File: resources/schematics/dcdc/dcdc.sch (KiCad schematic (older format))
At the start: 21 parts

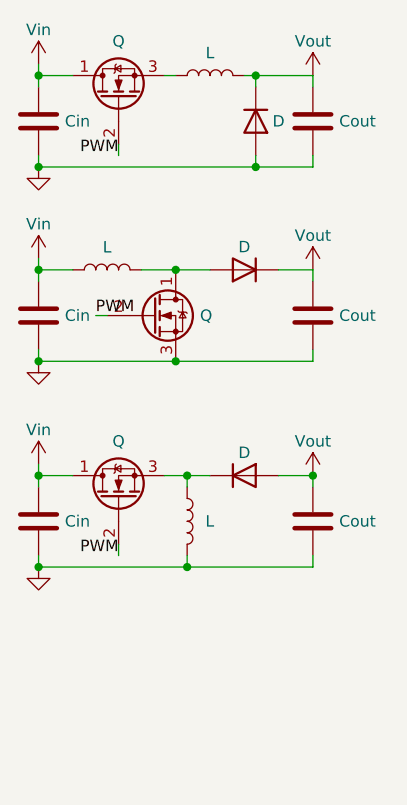
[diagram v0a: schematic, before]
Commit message: Add voltage divider diagram & minify svg
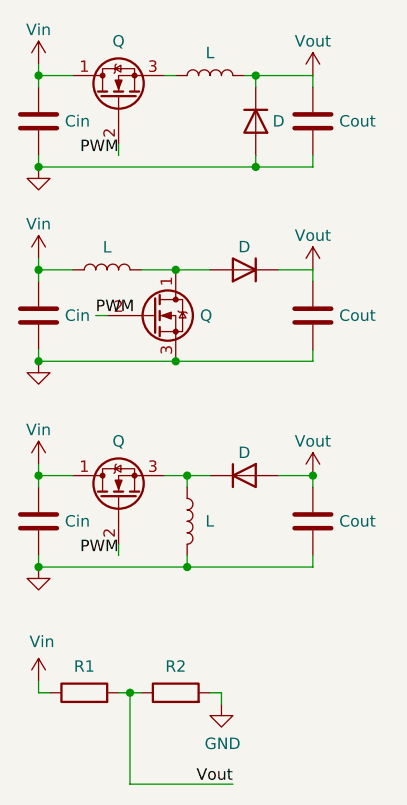
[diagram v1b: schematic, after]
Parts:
- added R1, R2: R, symbol Device:R
- added Vin: +12V, symbol power:+12V
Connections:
- net +12V: now also R1.1, Vin.1 (+12V)
- net GND: now also R2.2
- new net Vout: R1.2, R2.1
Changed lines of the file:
@@
 Connection ~ 650  2550
-$Comp
-L power:+12V Vin
-U 1 1 5DD46F62
-P 650 2500
-F 0 "Vin" H 650 2650 50  0000 C CNN
-F 1 "+12V" H 665 2673 50  0001 C CNN
-F 2 "" H 650 2500 50  0001 C CNN
-F 3 "" H 650 2500 50  0001 C CNN
-	1    650  2500
-	1    0    0    -1
-$EndComp
 $Comp
 L power:+12V Vout
@@
 	1    0    0    -1
 $EndComp
+$Comp
+L power:GND #PWR?
+U 1 1 5FDFFD01
+P 1450 3550
+F 0 "#PWR?" H 1450 3300 50  0001 C CNN
+F 1 "GND" H 1455 3377 50  0000 C CNN
+F 2 "" H 1450 3550 50  0001 C CNN
+F 3 "" H 1450 3550 50  0001 C CNN
+	1    1450 3550
+	1    0    0    -1
+$EndComp
+Wire Wire Line
+	1400 3500 1450 3500
+Wire Wire Line
+	1450 3500 1450 3550
+Wire Wire Line
+	700  3500 650  3500
+Wire Wire Line
+	650  3500 650  3450
+Wire Wire Line
+	1000 3500 1050 3500
+Wire Wire Line
+	1050 3500 1050 3900
+Wire Wire Line
+	1050 3900 1500 3900
+Connection ~ 1050 3500
+Wire Wire Line
+	1050 3500 1100 3500
+Text Label 1500 3900 2    50   ~ 0
+Vout
+$Comp
+L power:+12V Vin
+U 1 1 5DD46F62
+P 650 2500
+F 0 "Vin" H 650 2650 50  0000 C CNN
+F 1 "+12V" H 665 2673 50  0001 C CNN
+F 2 "" H 650 2500 50  0001 C CNN
+F 3 "" H 650 2500 50  0001 C CNN
+	1    650  2500
+	1    0    0    -1
+$EndComp
+$Comp
+L Device:R R2
+U 1 1 5FDFF45A
+P 1250 3500
+F 0 "R2" V 1365 3500 50  0000 C CNN
+F 1 "R" H 1320 3455 50  0001 L CNN
+F 2 "" V 1180 3500 50  0001 C CNN
+F 3 "~" H 1250 3500 50  0001 C CNN
+	1    1250 3500
+	0    -1   -1   0
+$EndComp
+$Comp
+L Device:R R1
+U 1 1 5FDFE9AA
+P 850 3500
+F 0 "R1" V 965 3500 50  0000 C CNN
+F 1 "R" H 920 3455 50  0001 L CNN
+F 2 "" V 780 3500 50  0001 C CNN
+F 3 "~" H 850 3500 50  0001 C CNN
+	1    850  3500
+	0    -1   -1   0
+$EndComp
+$Comp
+L power:+12V Vin
+U 1 1 5FE069E1
+P 650 3450
+F 0 "Vin" H 665 3623 50  0000 C CNN
+F 1 "+12V" H 665 3623 50  0001 C CNN
+F 2 "" H 650 3450 50  0001 C CNN
+F 3 "" H 650 3450 50  0001 C CNN
+	1    650  3450
+	1    0    0    -1
+$EndComp
